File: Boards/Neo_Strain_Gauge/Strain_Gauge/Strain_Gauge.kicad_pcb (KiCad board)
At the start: 2 copper layers, 85 x 56 mm, 71 parts, among them J1 Screw_Terminal_01x03, J2 Screw_Terminal_01x03, J3 Screw_Terminal_01x03, J4 Screw_Terminal_01x03, J5 Conn_01x02, J6 USB_B_Micro, J7 Conn_02x10_Counter_Clockwise, J8 Conn_02x12_Counter_Clockwise, U1 W25Q128JVS, U2 NCP1117-3.3_SOT223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

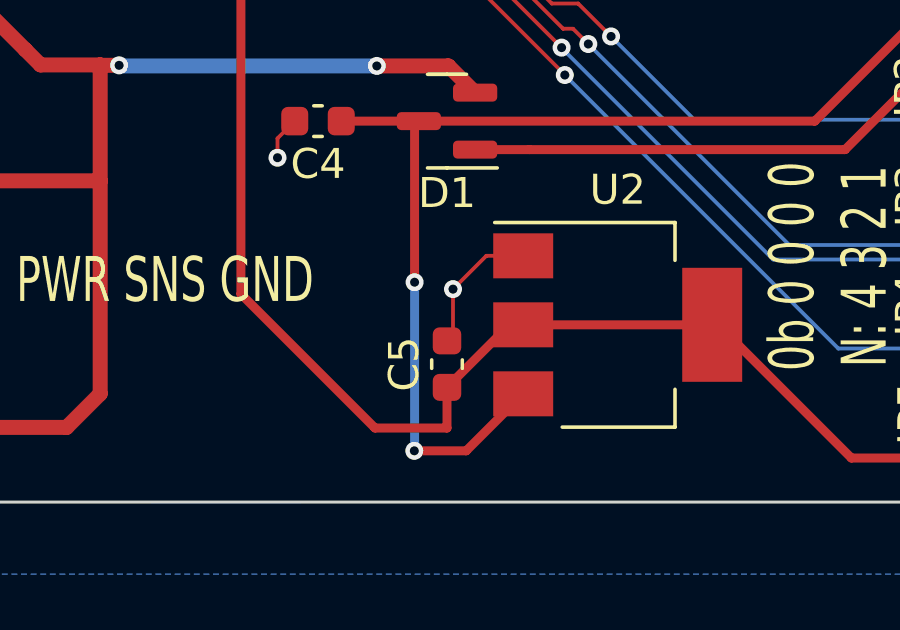
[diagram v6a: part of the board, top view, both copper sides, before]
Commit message: Replacement part due to parts shortage.
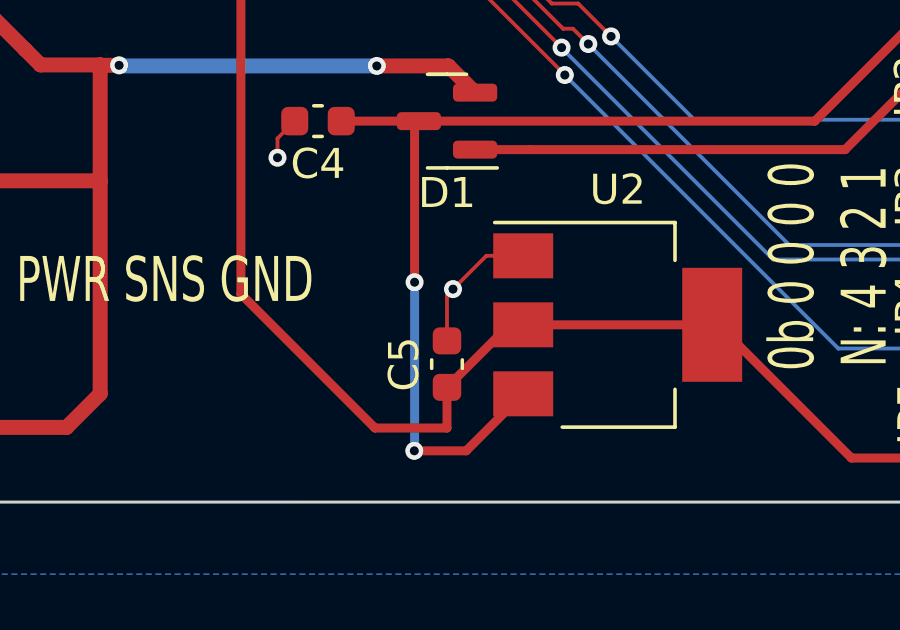
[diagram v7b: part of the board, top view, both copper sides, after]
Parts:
- C5: value 10u -> 22u
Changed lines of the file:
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@@
     (descr "Capacitor SMD 0603 (1608 Metric), square (rectangular) end terminal, IPC_7351 nominal, (Body size source: IPC-SM-782 page 76, https://www.pcb-3d.com/wordpress/wp-content/uploads/ipc-sm-782a_amendment_1_and_2.pdf), generated with kicad-footprint-generator")
     (tags "capacitor")
-    (property "Purchase Link" "https://www.digikey.com/en/products/detail/murata-electronics/GRT188C81A106ME13D/5416705")
+    (property "Purchase Link" "https://www.digikey.com/en/products/detail/samsung-electro-mechanics/CL10A226MP8NUNE/3886932")
     (property "Sheetfile" "Strain_Gauge.kicad_sch")
     (property "Sheetname" "")
@@
       (effects (font (size 1 1) (thickness 0.15)))
     )
-    (fp_text value "10u" (at 0 1.43 90) (layer "F.Fab")
+    (fp_text value "22u" (at 0 1.43 90) (layer "F.Fab")
       (effects (font (size 1 1) (thickness 0.15)))
     )
@@
     (descr "module CMS SOT223 4 pins")
     (tags "CMS SOT")
-    (property "Purchase Link" "https://www.digikey.com/en/products/detail/onsemi/NCP1117LPST33T3G/2194024")
+    (property "Purchase Link" "https://www.digikey.com/en/products/detail/dcomponents/LDI1117-3-3H/15850431")
     (property "Sheetfile" "Strain_Gauge.kicad_sch")
     (property "Sheetname" "")
@@
   (segment (start 131.35 81.75) (end 132.6 83) (width 0.127) (layer "F.Cu") (net 2))
   (segment (start 125.795 68.025) (end 125.79 68.02) (width 0.4) (layer "F.Cu") (net 2))
-  (segment (start 153.2 104.025) (end 153.2 102.5) (width 0.127) (layer "F.Cu") (net 2))
   (segment (start 170.795 106.57) (end 170.875 106.65) (width 0.127) (layer "F.Cu") (net 2))
   (segment (start 170.765 99.36) (end 170.795 99.39) (width 0.127) (layer "F.Cu") (net 2))
@@
   (segment (start 111.19 88.15) (end 111.17 88.17) (width 0.127) (layer "F.Cu") (net 2))
   (segment (start 132.53 76.29) (end 132.57 76.33) (width 0.127) (layer "F.Cu") (net 2))
+  (segment (start 153 102.7) (end 153.2 102.5) (width 0.127) (layer "F.Cu") (net 2))
   (segment (start 160 76.4375) (end 160 74.55) (width 0.127) (layer "F.Cu") (net 2))
   (segment (start 133.35 85.4375) (end 132.85 85.4375) (width 0.127) (layer "F.Cu") (net 2))
   (segment (start 133.375 74.44) (end 134.05 75.115) (width 0.127) (layer "F.Cu") (net 2))
   (segment (start 116.2 84.225) (end 116.2 82.9) (width 0.4) (layer "F.Cu") (net 2))
-  (segment (start 153 104.225) (end 153.2 104.025) (width 0.127) (layer "F.Cu") (net 2))
   (segment (start 132.385 73.32) (end 133.375 74.31) (width 0.127) (layer "F.Cu") (net 2))
   (segment (start 171.2375 56.05) (end 169.725 56.05) (width 0.127) (layer "F.Cu") (net 2))
@@
   (segment (start 169.48 72) (end 171 72) (width 0.127) (layer "F.Cu") (net 2))
   (segment (start 134.3365 85.424) (end 134.3365 84.7365) (width 0.127) (layer "F.Cu") (net 2))
+  (segment (start 153 104.225) (end 153 102.7) (width 0.127) (layer "F.Cu") (net 2))
   (segment (start 147.515 67.905) (end 147.4 67.905) (width 0.127) (layer "F.Cu") (net 2))
   (segment (start 133.35 83.75) (end 132.6 83) (width 0.127) (layer "F.Cu") (net 2))

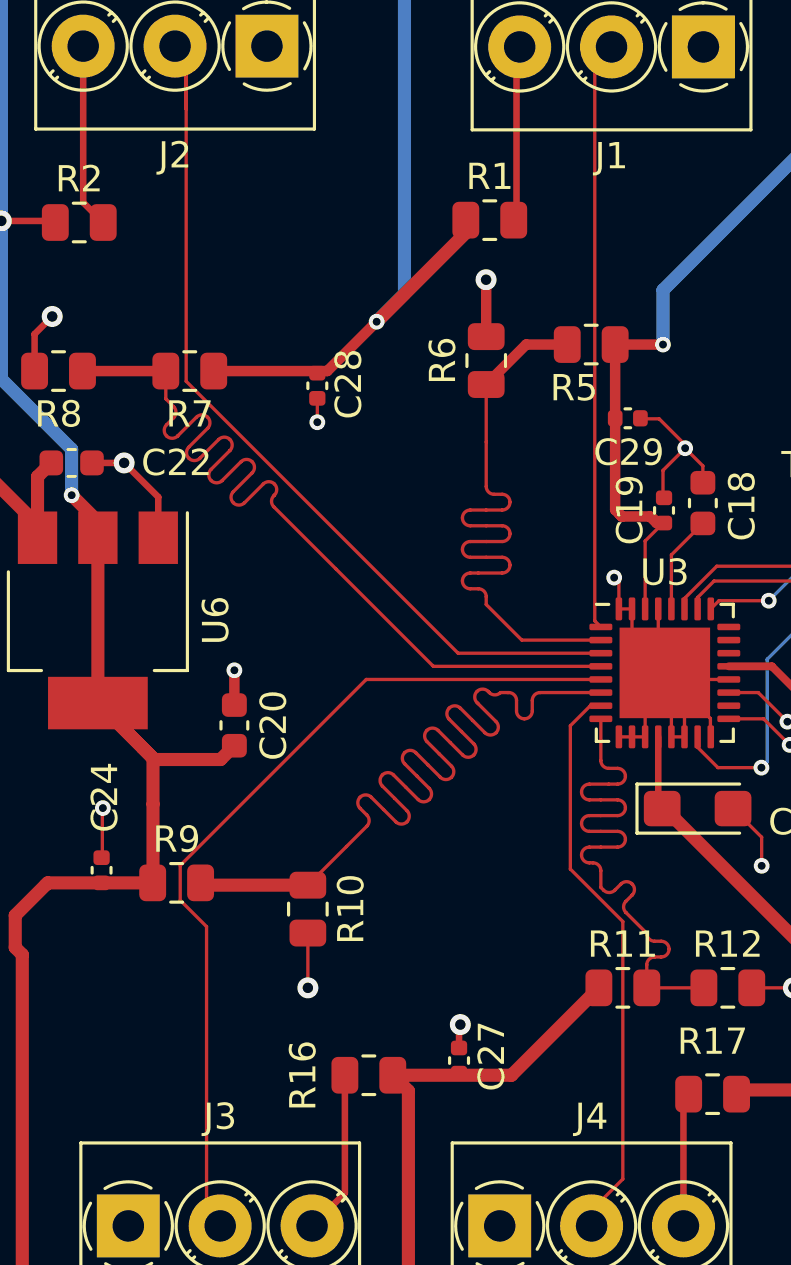
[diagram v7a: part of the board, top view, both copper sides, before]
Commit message: Make obvious what item is what in the SDAQ
Also add in my old headless DAQ code that is useful for non-attena constrained environments
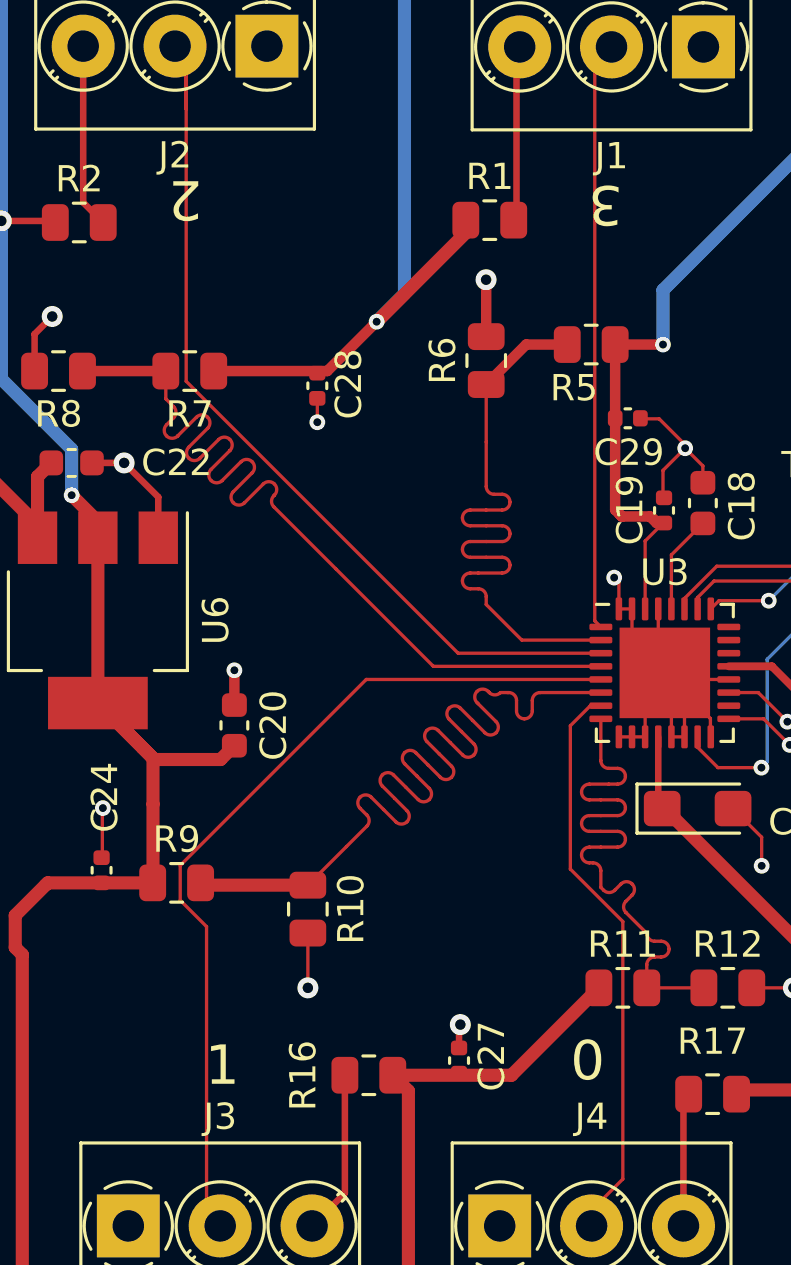
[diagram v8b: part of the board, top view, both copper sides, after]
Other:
- board text added: "0"
- board text added: "1"
- board text added: "2"
- board text added: "3"
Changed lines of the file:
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@@
     (effects (font (size 1.5 1) (thickness 0.125)))
+  )
+  (gr_text "1" (at 115.74 97.96) (layer "F.SilkS")
+    (effects (font (size 1.5 1.5) (thickness 0.3)))
+  )
+  (gr_text "2" (at 114.32 64.96 180) (layer "F.SilkS")
+    (effects (font (size 1.5 1.5) (thickness 0.3)))
+  )
+  (gr_text "0" (at 129.66 97.79) (layer "F.SilkS")
+    (effects (font (size 1.5 1.5) (thickness 0.3)))
+  )
+  (gr_text "3" (at 130.34 65.15 180) (layer "F.SilkS")
+    (effects (font (size 1.5 1.5) (thickness 0.3)))
   )
   (gr_text "PWR SNS GND" (at 144.6 58.7 180) (layer "F.SilkS")
